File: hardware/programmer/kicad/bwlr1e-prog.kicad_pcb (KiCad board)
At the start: 2 copper layers, 36.8 x 90.9 mm, 49 parts, among them J1 U262-161N-4BVC11, J2 PinHeader_1x08_P2.54mm_Horizo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, J3 PinHeader_1x02_P2.54mm_Horizo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, J4 PinHeader_1x02_P2.54mm_Horizo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, Q1 AO3407A, SW1 A6H-4101, SW2 TL3342F160QG, SW3 TL3342F160QG, U1 MCP73831T-2ACI/OT, U2 USBLC6-2P6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

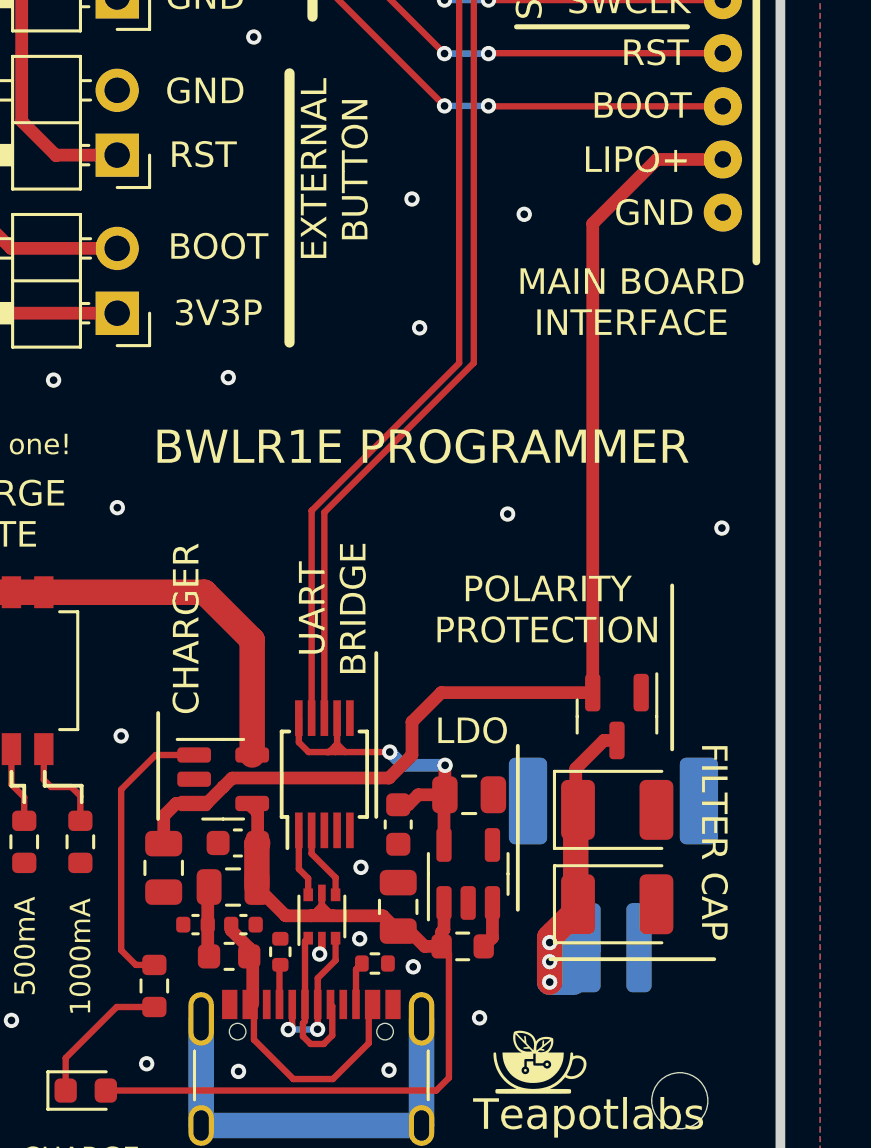
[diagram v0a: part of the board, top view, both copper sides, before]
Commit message: move batt jst to top and change to rev 2
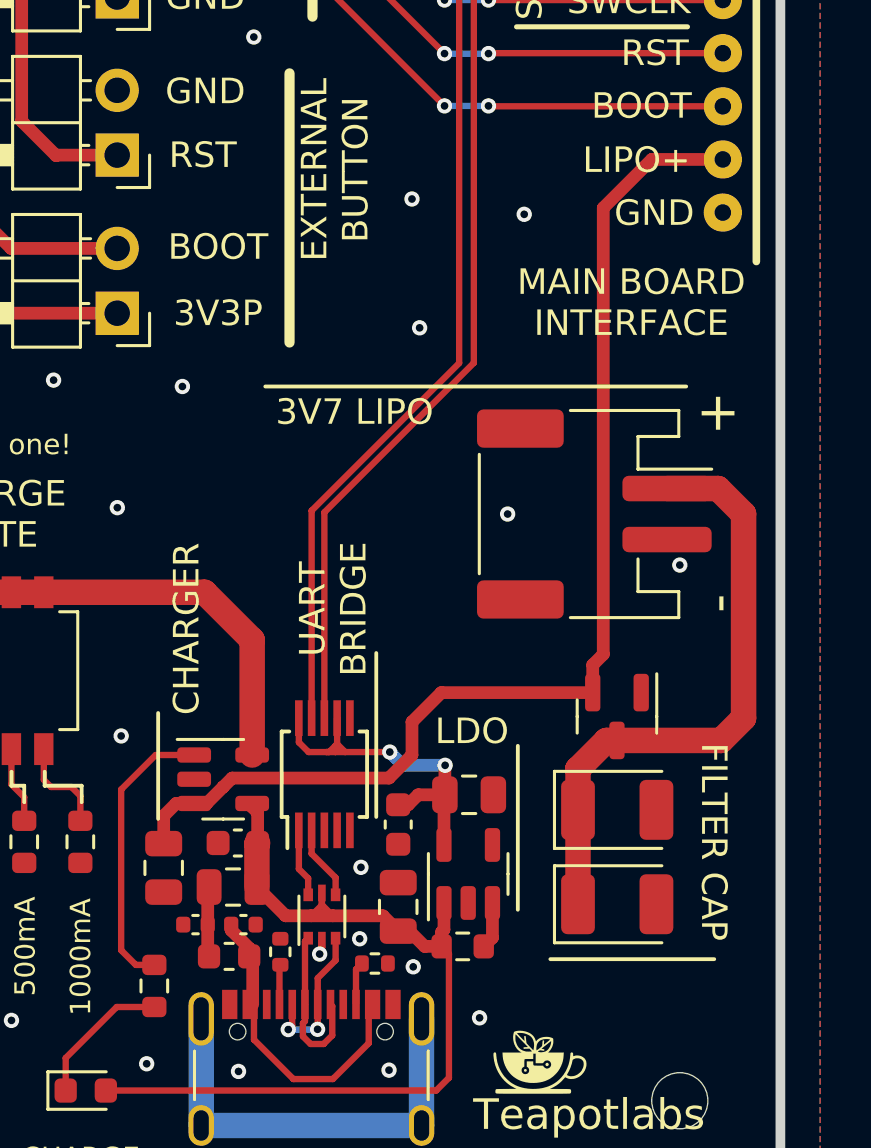
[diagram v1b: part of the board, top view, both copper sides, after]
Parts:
- BT1: moved to F.Cu
- moved BT1 14.2 mm to (157.7, 117.0), turned to -90 degrees
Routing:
- net Net-(BT1-+): track 16.7 -> 24.0 mm, vias 3 -> 0
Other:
- board text added: "REVISION 2"
- board text removed: "POLARITY PROTECTION"
- board text removed: "REVISION 1"

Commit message: improve usb diff pair and change to rev 3
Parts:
- moved U4 1.70 mm to (147.1, 128.9)
- moved U2 0.82 mm to (147.0, 133.6)
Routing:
- net +BATT: track 45.3 -> 54.7 mm, vias 0 -> 4
- net +3V3: track 14.5 -> 11.7 mm, vias 2 -> 0
- net VBUS: track 34.4 -> 36.4 mm, vias 0 -> 2
- net /TXD2: track 62.0 -> 63.7 mm
- net /RXD2: track 66.9 -> 68.6 mm
- net /D+: track 2.68 -> 1.80 mm
- net /D_IN-: track 6.07 -> 5.24 mm
- net /D_IN+: track 6.59 -> 5.89 mm
- net GND: track 0.58 -> 0.00 mm, vias 31 -> 30
- net /D-: track 2.92 -> 2.40 mm
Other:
- board text added: "REVISION 3"
- board text added: "USB-UART BRIDGE"
- board text removed: "REVISION 2"
- board text removed: "UART BRIDGE"

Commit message: add marker for pcb blender export
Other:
- board text added: "PCB3D_BR_bwlr1e-prog"
- board text added: "PCB3D_TL_bwlr1e-prog"
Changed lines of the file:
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@@
     (effects (font (size 0.5 0.5) (thickness 0.125)))
+  )
+  (gr_text "PCB3D_TL_bwlr1e-prog" (at 127.69 52.34) (layer "F.Fab")
+    (effects (font (size 2 2) (thickness 0.3)) (justify left bottom))
   )
   (gr_text "TP8" (at 164 88.5 -90) (layer "F.Fab")
     (effects (font (size 0.5 0.5) (thickness 0.125)))
   )
+  (gr_text "PCB3D_BR_bwlr1e-prog" (at 165.68 144.77) (layer "F.Fab")
+    (effects (font (size 2 2) (thickness 0.3)) (justify left bottom))
+  )
   (gr_text "TP4" (at 163.987 90.6 -90) (layer "F.Fab")
